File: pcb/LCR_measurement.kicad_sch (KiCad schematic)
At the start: 53 parts, among them J3 Conn_01x04_Socket, J4 Conn_01x01_Pin, J5 Conn_01x01_Pin, SW2 SW_DIP_x02, SW3 SW_SPST, U3 AT24CM02-SSHM, U4 ATtiny1604-SS, U5 MCP2221AxSL, U6 MCP4921, U7 MCP6001-OT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

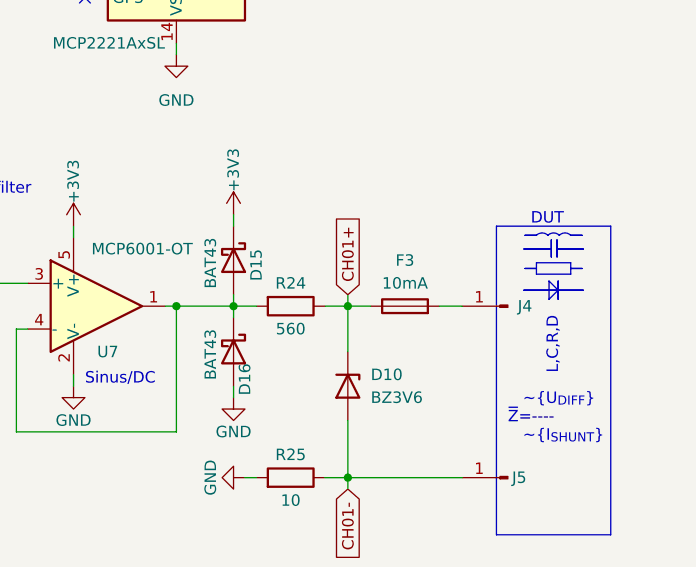
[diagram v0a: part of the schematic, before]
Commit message: Add/fix missing/wrong vendor(id)
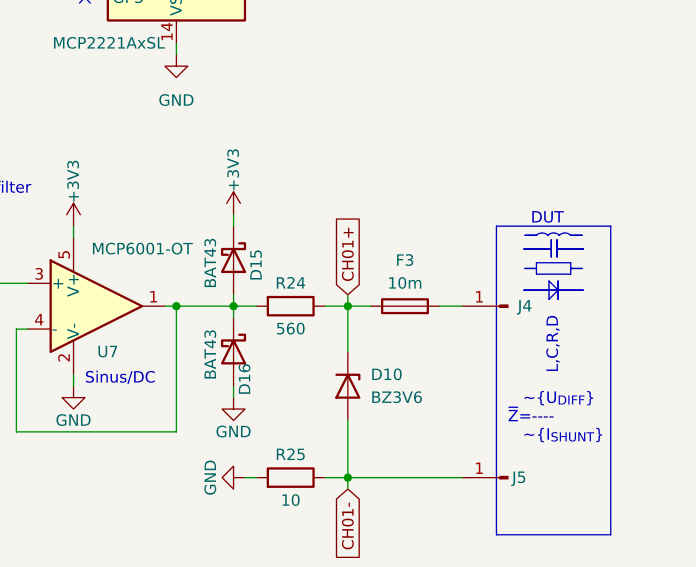
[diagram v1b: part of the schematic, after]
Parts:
- C22: VendorId 100128 -> 103341
- D10: Vendor (none) -> HTL; VendorId (none) -> 100188
- D11, D12, D13, D14, D15, D16, D6, D7, D8, D9: Vendor (none) -> HTL; VendorId (none) -> 100206
- F3: value 10mA -> 10m
- J3: Vendor HTL -> Amazon; VendorId 101546 -> B07BDFXFRK
- R12, R18: VendorId 102944 -> 102967
- R24: VendorId 102951 -> 102945
- R25: VendorId 102951 -> 102913
- SW3: Vendor (none) -> HTL; VendorId (none) -> 101614
- U6: Vendor (none) -> DigiKey; VendorId (none) -> MCP4921T-E/MSCT-ND
- U7: Vendor (none) -> DigiKey; VendorId (none) -> MCP6001T-I/OTCT-ND
- U8: Vendor (none) -> DigiKey; VendorId (none) -> 150-MCP3562RT-E/STCT-ND
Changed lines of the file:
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@@
       (effects (font (size 1.27 1.27)) hide)
     )
-    (property "VendorId" "102944" (at 156.21 74.93 0)
+    (property "VendorId" "102967" (at 156.21 74.93 0)
       (effects (font (size 1.27 1.27)) hide)
     )
@@
       (effects (font (size 1.27 1.27)) hide)
     )
+    (property "Vendor" "HTL" (at 63.5 138.43 0)
+      (effects (font (size 1.27 1.27)) hide)
+    )
+    (property "VendorId" "100206" (at 63.5 138.43 0)
+      (effects (font (size 1.27 1.27)) hide)
+    )
     (pin "1")
     (pin "2")
@@
       (effects (font (size 1.27 1.27)) hide)
     )
+    (property "Vendor" "HTL" (at 43.18 123.19 0)
+      (effects (font (size 1.27 1.27)) hide)
+    )
+    (property "VendorId" "100206" (at 43.18 123.19 0)
+      (effects (font (size 1.27 1.27)) hide)
+    )
     (pin "1")
     (pin "2")
@@
     )
     (property "Datasheet" "~" (at 218.44 123.19 0)
+      (effects (font (size 1.27 1.27)) hide)
+    )
+    (property "Vendor" "HTL" (at 218.44 123.19 0)
+      (effects (font (size 1.27 1.27)) hide)
+    )
+    (property "VendorId" "100206" (at 218.44 123.19 0)
       (effects (font (size 1.27 1.27)) hide)
     )
@@
       (effects (font (size 1.27 1.27)) hide)
     )
-    (property "VendorId" "102944" (at 156.21 64.77 0)
+    (property "VendorId" "102967" (at 156.21 64.77 0)
       (effects (font (size 1.27 1.27)) hide)
     )
@@
       (effects (font (size 1.27 1.27)) hide)
     )
-    (property "Vendor" "HTL" (at 66.04 77.47 0)
-      (effects (font (size 1.27 1.27)) hide)
-    )
-    (property "VendorId" "101546" (at 66.04 77.47 0)
+    (property "Vendor" "Amazon" (at 66.04 77.47 0)
+      (effects (font (size 1.27 1.27)) hide)
+    )
+    (property "VendorId" "B07BDFXFRK" (at 66.04 77.47 0)
       (effects (font (size 1.27 1.27)) hide)
     )
@@
       (effects (font (size 1.27 1.27)) hide)
     )
-    (property "VendorId" "102951" (at 224.79 137.16 0)
+    (property "VendorId" "102913" (at 224.79 137.16 0)
       (effects (font (size 1.27 1.27)) hide)
     )
@@
       (effects (font (size 1.27 1.27)) hide)
     )
+    (property "Vendor" "HTL" (at 33.02 123.19 0)
+      (effects (font (size 1.27 1.27)) hide)
+    )
+    (property "VendorId" "100206" (at 33.02 123.19 0)
+      (effects (font (size 1.27 1.27)) hide)
+    )
     (pin "1")
     (pin "2")
@@
       (effects (font (size 1.27 1.27)) hide)
     )
+    (property "Vendor" "HTL" (at 43.18 130.81 0)
+      (effects (font (size 1.27 1.27)) hide)
+    )
+    (property "VendorId" "100206" (at 43.18 130.81 0)
+      (effects (font (size 1.27 1.27)) hide)
+    )
     (pin "1")
     (pin "2")
@@
     )
     (property "Datasheet" "~" (at 218.44 113.03 0)
+      (effects (font (size 1.27 1.27)) hide)
+    )
+    (property "Vendor" "HTL" (at 218.44 113.03 0)
+      (effects (font (size 1.27 1.27)) hide)
+    )
+    (property "VendorId" "100206" (at 218.44 113.03 0)
       (effects (font (size 1.27 1.27)) hide)
     )
@@
       (effects (font (size 1.27 1.27)))
     )
-    (property "Value" "10mA" (at 237.49 115.57 90)
+    (property "Value" "10m" (at 237.49 115.57 90)
       (effects (font (size 1.27 1.27)))
     )
@@
     )
     (property "Datasheet" "~" (at 53.34 115.57 0)
+      (effects (font (size 1.27 1.27)) hide)
+    )
+    (property "Vendor" "HTL" (at 53.34 115.57 0)
+      (effects (font (size 1.27 1.27)) hide)
+    )
+    (property "VendorId" "100206" (at 53.34 115.57 0)
       (effects (font (size 1.27 1.27)) hide)
     )
@@
     )
     (property "Datasheet" "http://ww1.microchip.com/downloads/en/DeviceDoc/21733j.pdf" (at 203.2 113.03 0)
+      (effects (font (size 1.27 1.27)) hide)
+    )
+    (property "Vendor" "DigiKey" (at 203.2 118.11 0)
+      (effects (font (size 1.27 1.27)) hide)
+    )
+    (property "VendorId" "MCP6001T-I/OTCT-ND" (at 203.2 118.11 0)
       (effects (font (size 1.27 1.27)) hide)
     )
@@
       (effects (font (size 1.27 1.27)) hide)
     )
+    (property "Vendor" "HTL" (at 63.5 115.57 0)
+      (effects (font (size 1.27 1.27)) hide)
+    )
+    (property "VendorId" "100206" (at 63.5 115.57 0)
+      (effects (font (size 1.27 1.27)) hide)
+    )
     (pin "1")
     (pin "2")
@@
     (property "Datasheet" "MCP3562RT-E/ST" (at 110.49 121.92 0)
       (effects (font (size 1.27 1.27) italic) hide)
+    )
+    (property "Vendor" "DigiKey" (at 110.49 121.92 0)
+      (effects (font (size 1.27 1.27)) hide)
+    )
+    (property "VendorId" "150-MCP3562RT-E/STCT-ND" (at 110.49 121.92 0)
+      (effects (font (size 1.27 1.27)) hide)
     )
     (pin "4")
@@
       (effects (font (size 1.27 1.27)) hide)
     )
+    (property "Vendor" "DigiKey" (at 160.02 115.57 0)
+      (effects (font (size 1.27 1.27)) hide)
+    )
+    (property "VendorId" "MCP4921T-E/MSCT-ND" (at 160.02 115.57 0)
+      (effects (font (size 1.27 1.27)) hide)
+    )
     (pin "5")
     (pin "7")
@@
       (effects (font (size 1.27 1.27)) hide)
     )
+    (property "Vendor" "HTL" (at 134.62 77.47 0)
+      (effects (font (size 1.27 1.27)) hide)
+    )
+    (property "VendorId" "101614" (at 134.62 77.47 0)
+      (effects (font (size 1.27 1.27)) hide)
+    )
     (pin "2")
     (pin "1")
@@
       (effects (font (size 1.27 1.27)) hide)
     )
+    (property "Vendor" "HTL" (at 53.34 138.43 0)
+      (effects (font (size 1.27 1.27)) hide)
+    )
+    (property "VendorId" "100206" (at 53.34 138.43 0)
+      (effects (font (size 1.27 1.27)) hide)
+    )
     (pin "1")
     (pin "2")
@@
     )
     (property "Datasheet" "~" (at 33.02 130.81 0)
+      (effects (font (size 1.27 1.27)) hide)
+    )
+    (property "Vendor" "HTL" (at 33.02 130.81 0)
+      (effects (font (size 1.27 1.27)) hide)
+    )
+    (property "VendorId" "100206" (at 33.02 130.81 0)
       (effects (font (size 1.27 1.27)) hide)
     )
@@
       (effects (font (size 1.27 1.27)) hide)
     )
+    (property "Vendor" "HTL" (at 231.14 127 0)
+      (effects (font (size 1.27 1.27)) hide)
+    )
+    (property "VendorId" "100188" (at 231.14 127 0)
+      (effects (font (size 1.27 1.27)) hide)
+    )
     (pin "1")
     (pin "2")
@@
       (effects (font (size 1.27 1.27)) hide)
     )
-    (property "VendorId" "102951" (at 224.79 118.11 0)
+    (property "VendorId" "102945" (at 224.79 118.11 0)
       (effects (font (size 1.27 1.27)) hide)
     )
@@
       (effects (font (size 1.27 1.27)) hide)
     )
-    (property "VendorId" "100128" (at 187.96 120.65 0)
-      (effects (font (size 1.27 1.27)) hide)
-    )
+    (property "VendorId" "103341" (at 187.96 120.65 0)
+      (effects (font (size 1.27 1.27)) hide)
+    )

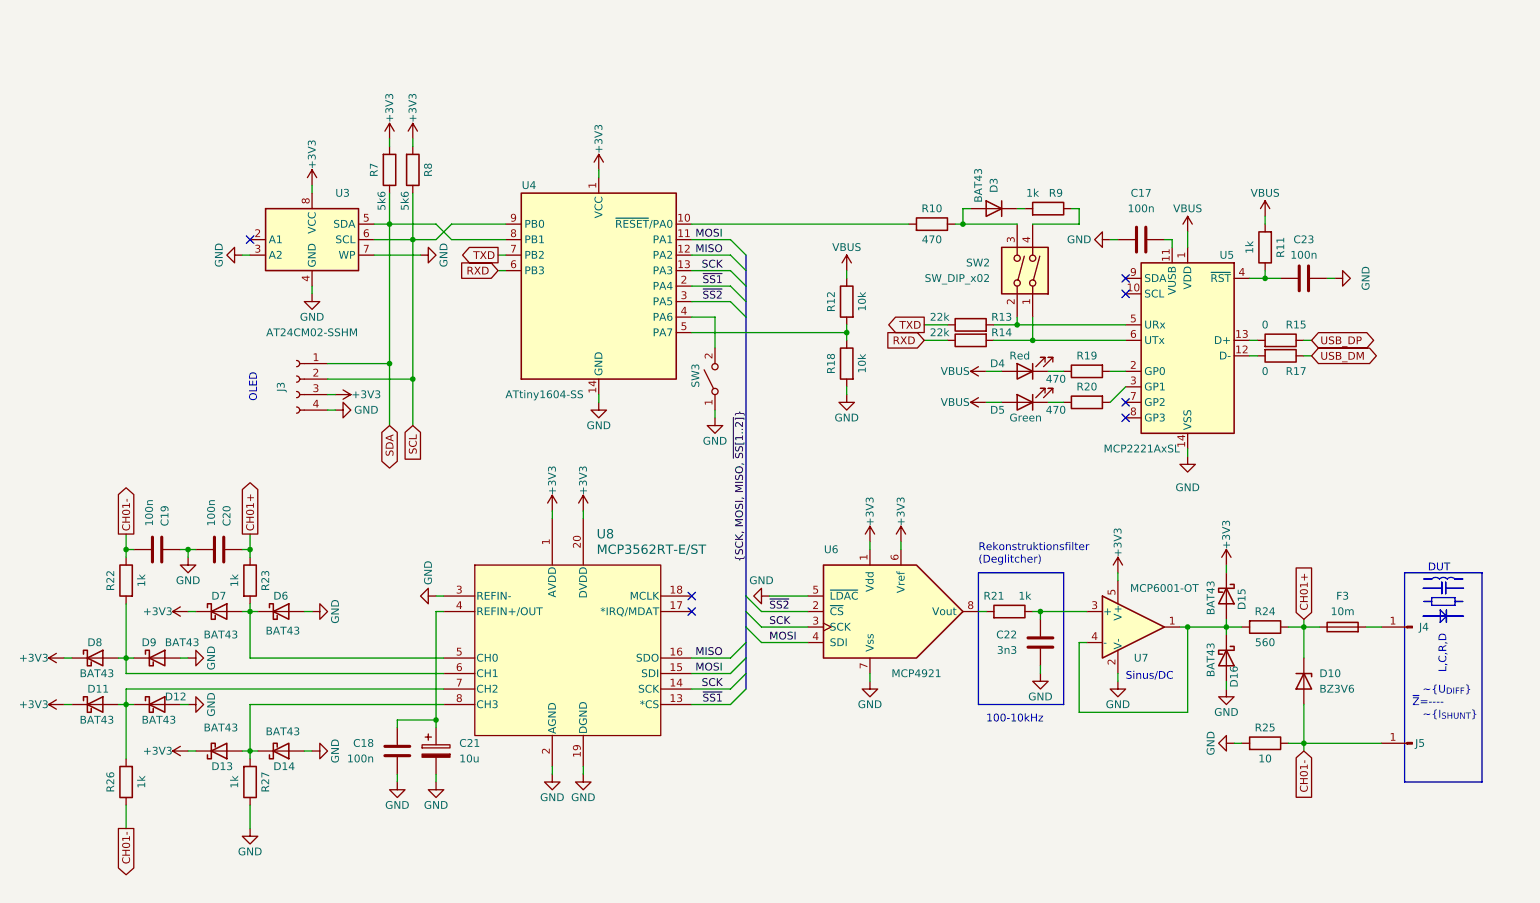
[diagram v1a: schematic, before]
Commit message: Change MCP2221A to FT230X
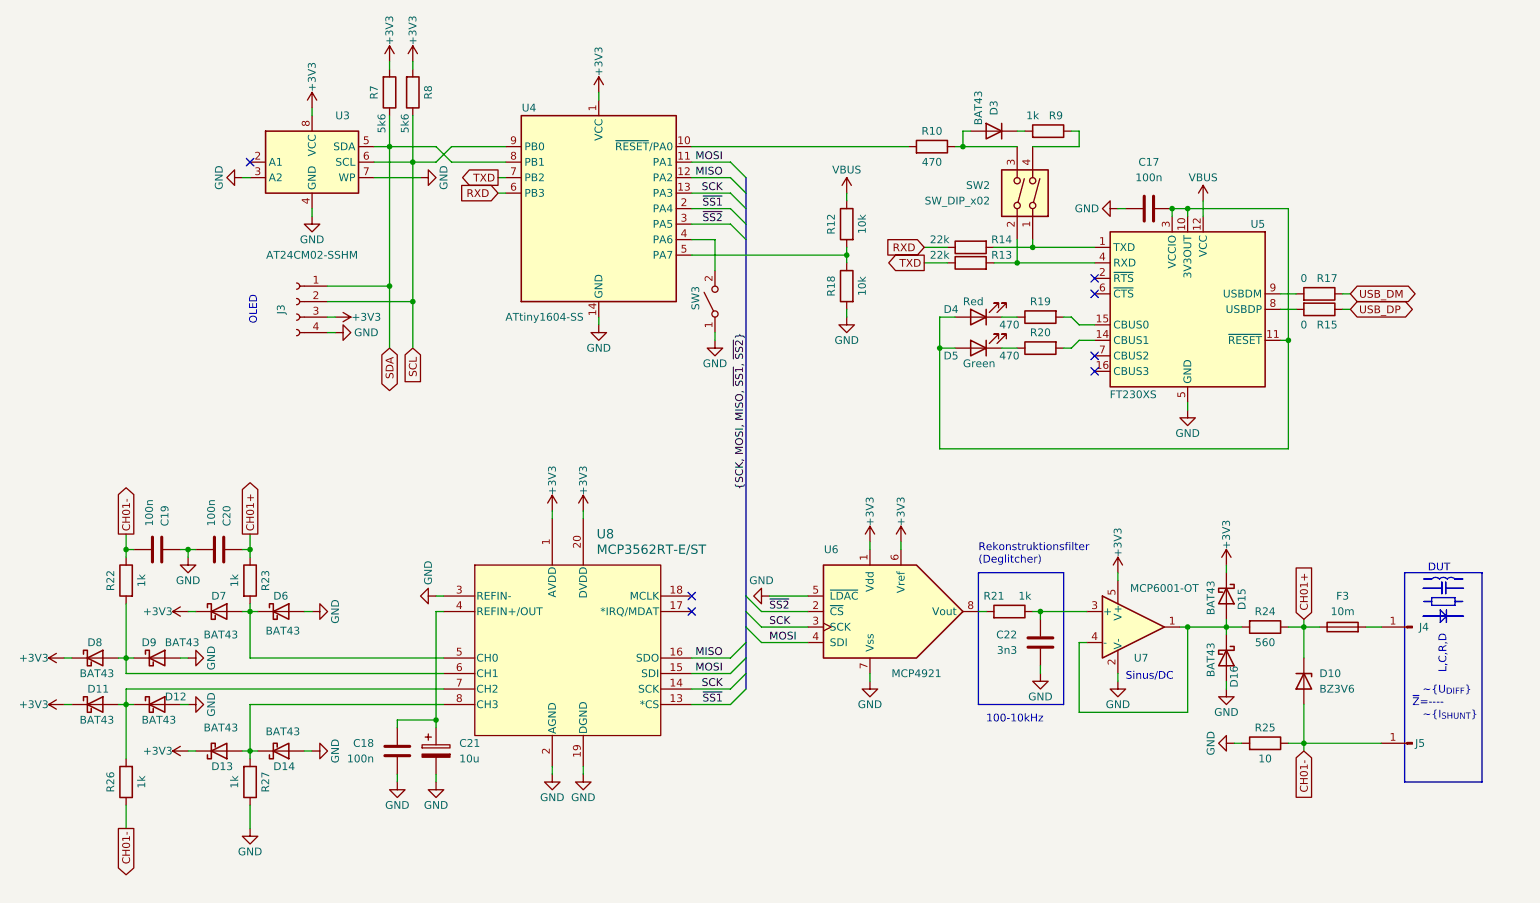
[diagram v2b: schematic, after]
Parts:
- removed C23: 100n, Capacitor_SMD:C_1206_3216Metric, symbol Device:C
- removed R11: 1k, Resistor_SMD:R_1206_3216Metric, symbol Device:R
- removed U5: MCP2221AxSL, Package_SO:SOIC-14_3.9x8.7mm_P1.27mm, symbol Interface_USB:MCP2221AxSL
- added U5: FT230XS, Package_SO:SSOP-16_3.9x4.9mm_P0.635mm, symbol Interface_USB:FT230XS
- C17: HTL (none) -> 100128; Vendor HTL -> (none); VendorId 100128 -> (none)
- D4: HTL (none) -> 100458; Vendor HTL -> (none); VendorId 100458 -> (none)
- D5: HTL (none) -> 100459; Vendor HTL -> (none); VendorId 100459 -> (none)
- R15, R17: DigiKey (none) -> RMCF0603ZT0R00CT-ND; Vendor DigiKey -> (none); VendorId RMCF0603ZT0R00CT-ND -> (none)
- R19, R20: HTL (none) -> 102944; Vendor HTL -> (none); VendorId 102944 -> (none)
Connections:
- net GND: now also U5.13 (GND), U5.5 (GND)
- net VBUS: now also U5.12 (VCC); no longer D4.2 (A), D5.2 (A)
- net at C17.1: now also D4.2 (A), D5.2 (A), U5.10 (3V3OUT), U5.11 (~{RESET}), U5.3 (VCCIO)
- net at R14.2, SW2.1: now also U5.1 (TXD)
- net at R13.2, SW2.2: now also U5.4 (RXD)
- net at R15.2: now also U5.8 (USBDP)
- net at R20.2: now also U5.14 (CBUS1)
- net at R17.2: now also U5.9 (USBDM)
- net at R19.2: now also U5.15 (CBUS0)
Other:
- moved on the sheet: D3, J3, R10, R12, R13, R14, R18, R7, R8, R9, SW2, SW3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

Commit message: Rename/Add/Remove bom fields
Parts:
- C18, C19, C20: HTL (none) -> 100128; Vendor HTL -> (none); VendorId 100128 -> (none)
- C21: HTL (none) -> 103620; Vendor HTL -> (none); VendorId 103620 -> (none)
- C22: HTL (none) -> 103341; Vendor HTL -> (none); VendorId 103341 -> (none)
- D10: HTL (none) -> 100188; Vendor HTL -> (none); VendorId 100188 -> (none)
- D11, D12, D13, D14, D15, D16, D3, D6, D7, D8, D9: HTL (none) -> 100206; Vendor HTL -> (none); VendorId 100206 -> (none)
- F3: DigiKey (none) -> 18-0603L001/60YRCT-ND; Vendor DigiKey -> (none); VendorId 18-0603L001/60YRCT-ND -> (none)
- J3: Amazon (none) -> B07BDFXFRK; Vendor Amazon -> (none); VendorId B07BDFXFRK -> (none)
- J4, J5: now left out of the parts list
- R10: HTL (none) -> 102944; Vendor HTL -> (none); VendorId 102944 -> (none)
- R12, R18: HTL (none) -> 102967; Vendor HTL -> (none); VendorId 102967 -> (none)
- R13, R14: HTL (none) -> 102973; Vendor HTL -> (none); VendorId 102973 -> (none)
- R21, R22, R23, R26, R27, R9: HTL (none) -> 102951; Vendor HTL -> (none); VendorId 102951 -> (none)
- R24: HTL (none) -> 102945; Vendor HTL -> (none); VendorId 102945 -> (none)
- R25: HTL (none) -> 102913; Vendor HTL -> (none); VendorId 102913 -> (none)
- R7, R8: HTL (none) -> 102963; Vendor HTL -> (none); VendorId 102963 -> (none)
- SW2: HTL (none) -> 103604; Vendor HTL -> (none); VendorId 103604 -> (none)
- SW3: HTL (none) -> 101614; Vendor HTL -> (none); VendorId 101614 -> (none)
- U3: HTL (none) -> 103616; Vendor HTL -> (none); VendorId 103616 -> (none)
- U4: HTL (none) -> 103615; Vendor HTL -> (none); VendorId 103615 -> (none)
- U6: DigiKey (none) -> MCP4921T-E/MSCT-ND; Vendor DigiKey -> (none); VendorId MCP4921T-E/MSCT-ND -> (none)
- U7: DigiKey (none) -> MCP6001T-I/OTCT-ND; Vendor DigiKey -> (none); VendorId MCP6001T-I/OTCT-ND -> (none)
- U8: DigiKey (none) -> 150-MCP3562RT-E/STCT-ND; Vendor DigiKey -> (none); VendorId 150-MCP3562RT-E/STCT-ND -> (none)
